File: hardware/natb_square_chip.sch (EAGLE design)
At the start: 8 parts, among them U1 TINY212, U2 MEGA32U4-MU

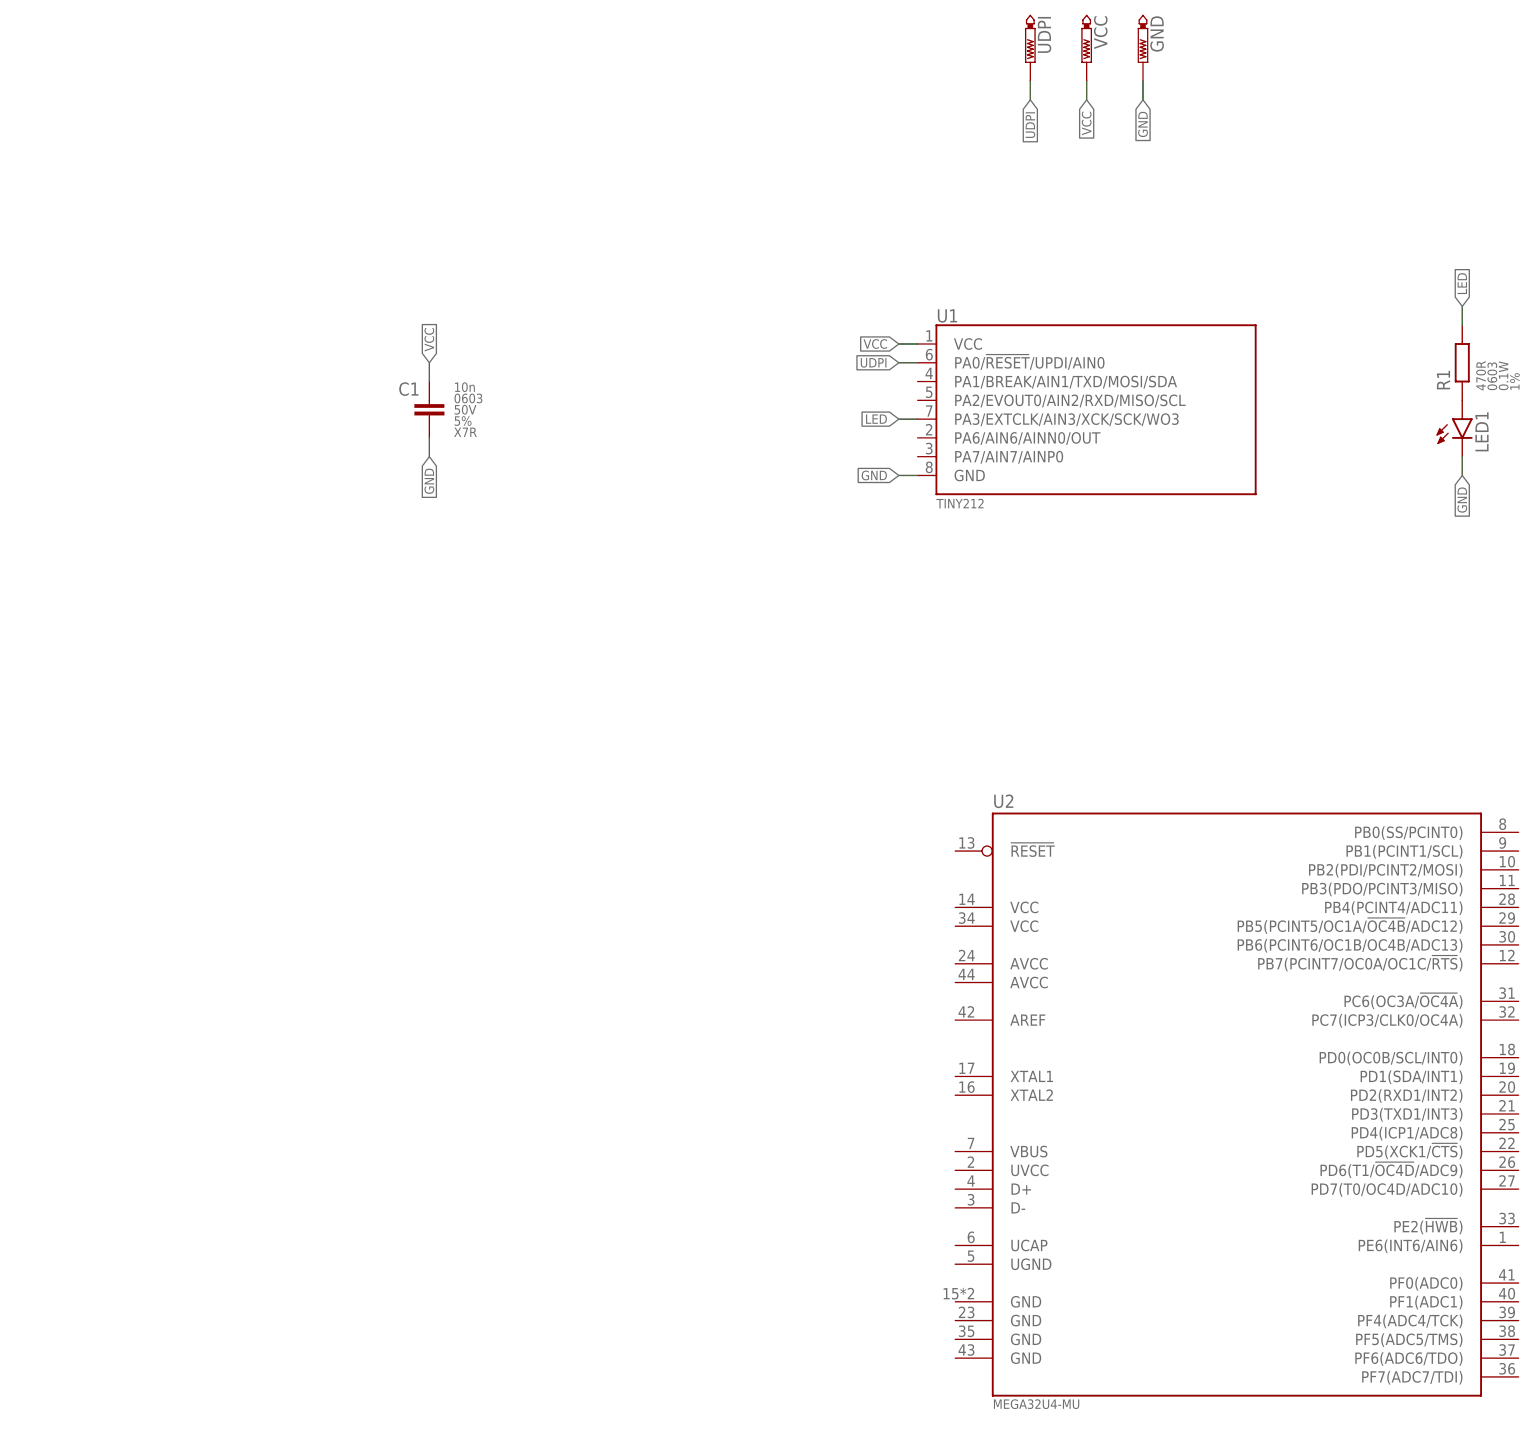
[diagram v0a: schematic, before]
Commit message: Changes SOIC and BGA
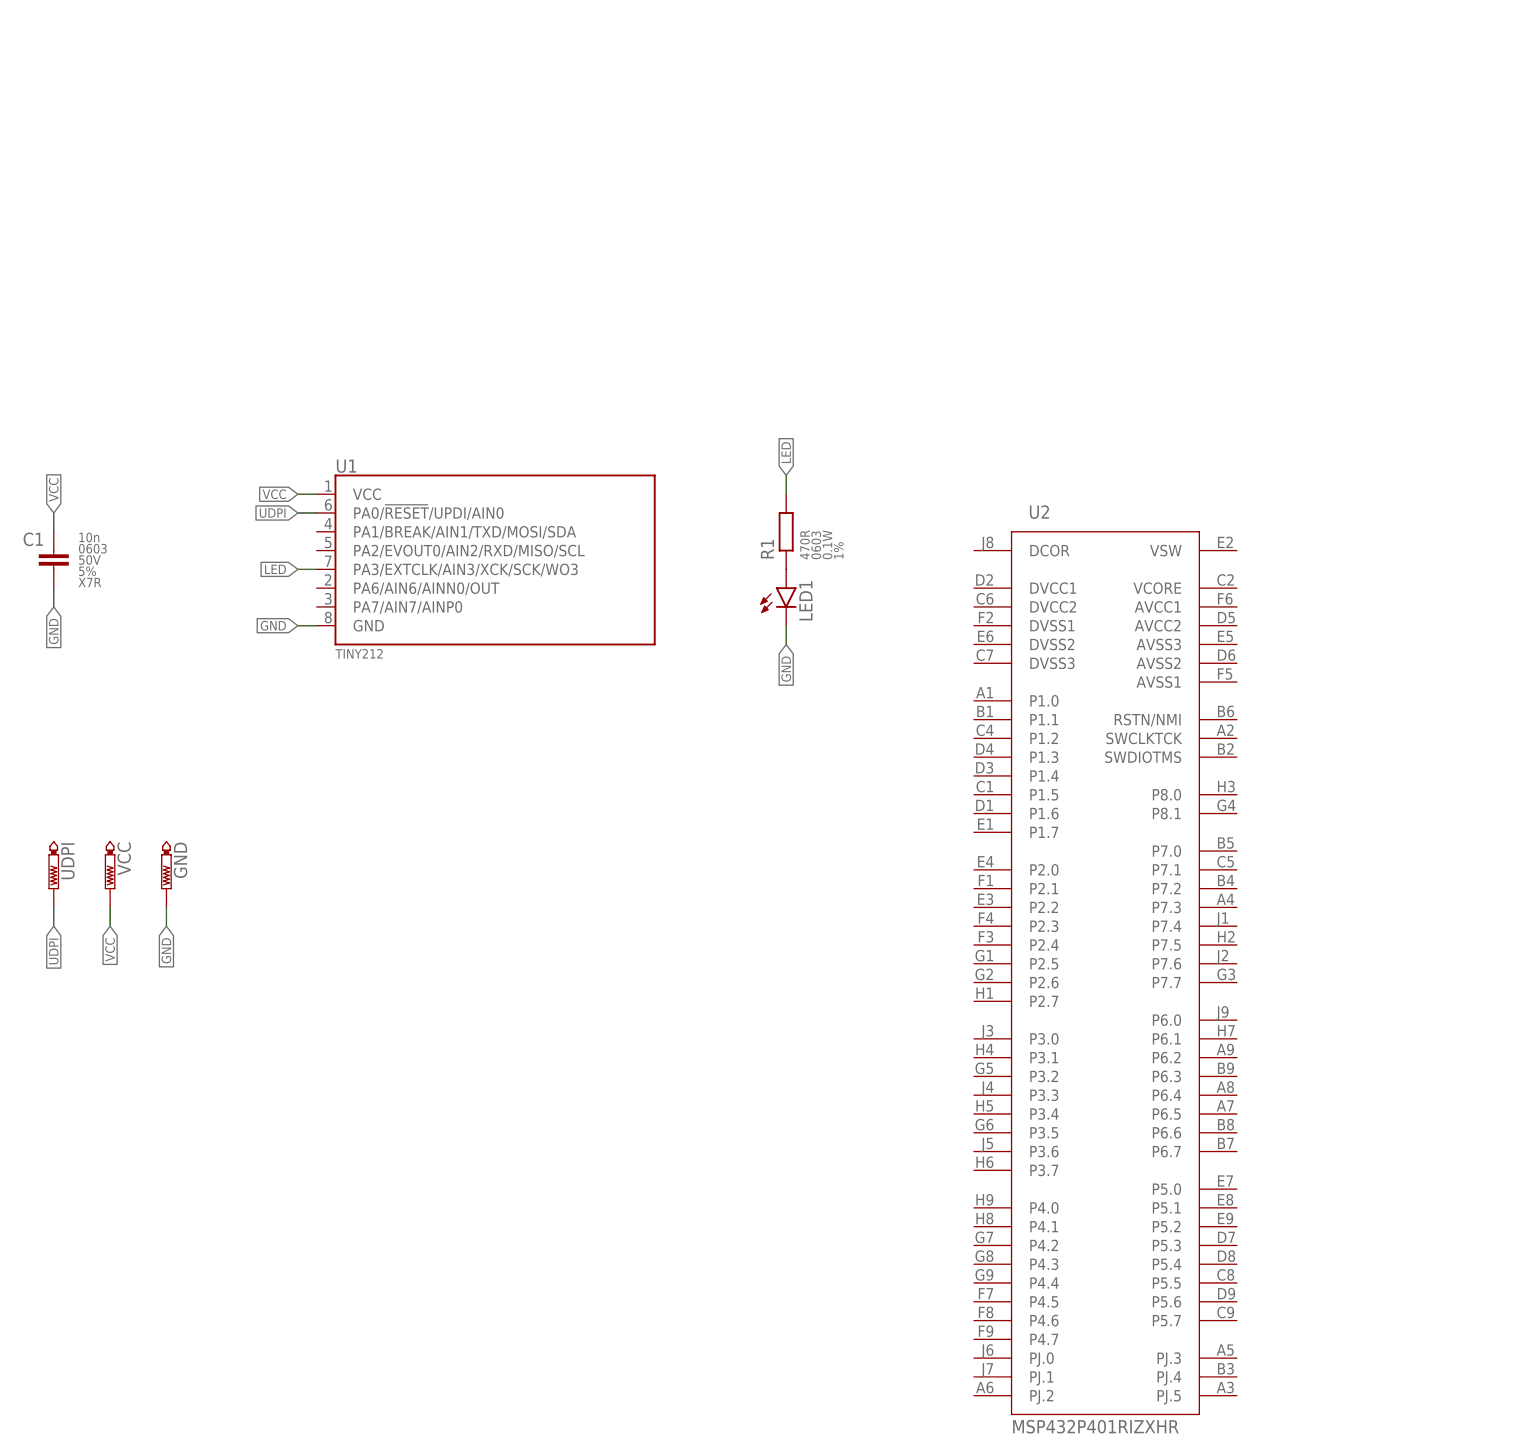
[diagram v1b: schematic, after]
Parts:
- U2: value MEGA32U4-MU -> MSP432P401RIZXHR; device zaan-IC-Microcontroller:MEGA32U4-MU -> Microcontroller:MSP432P401RIZXHR
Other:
- moved on the sheet: C1, GND, LED1, R1, U1, UDPI, VCC

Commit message: Changed parts and added qr code
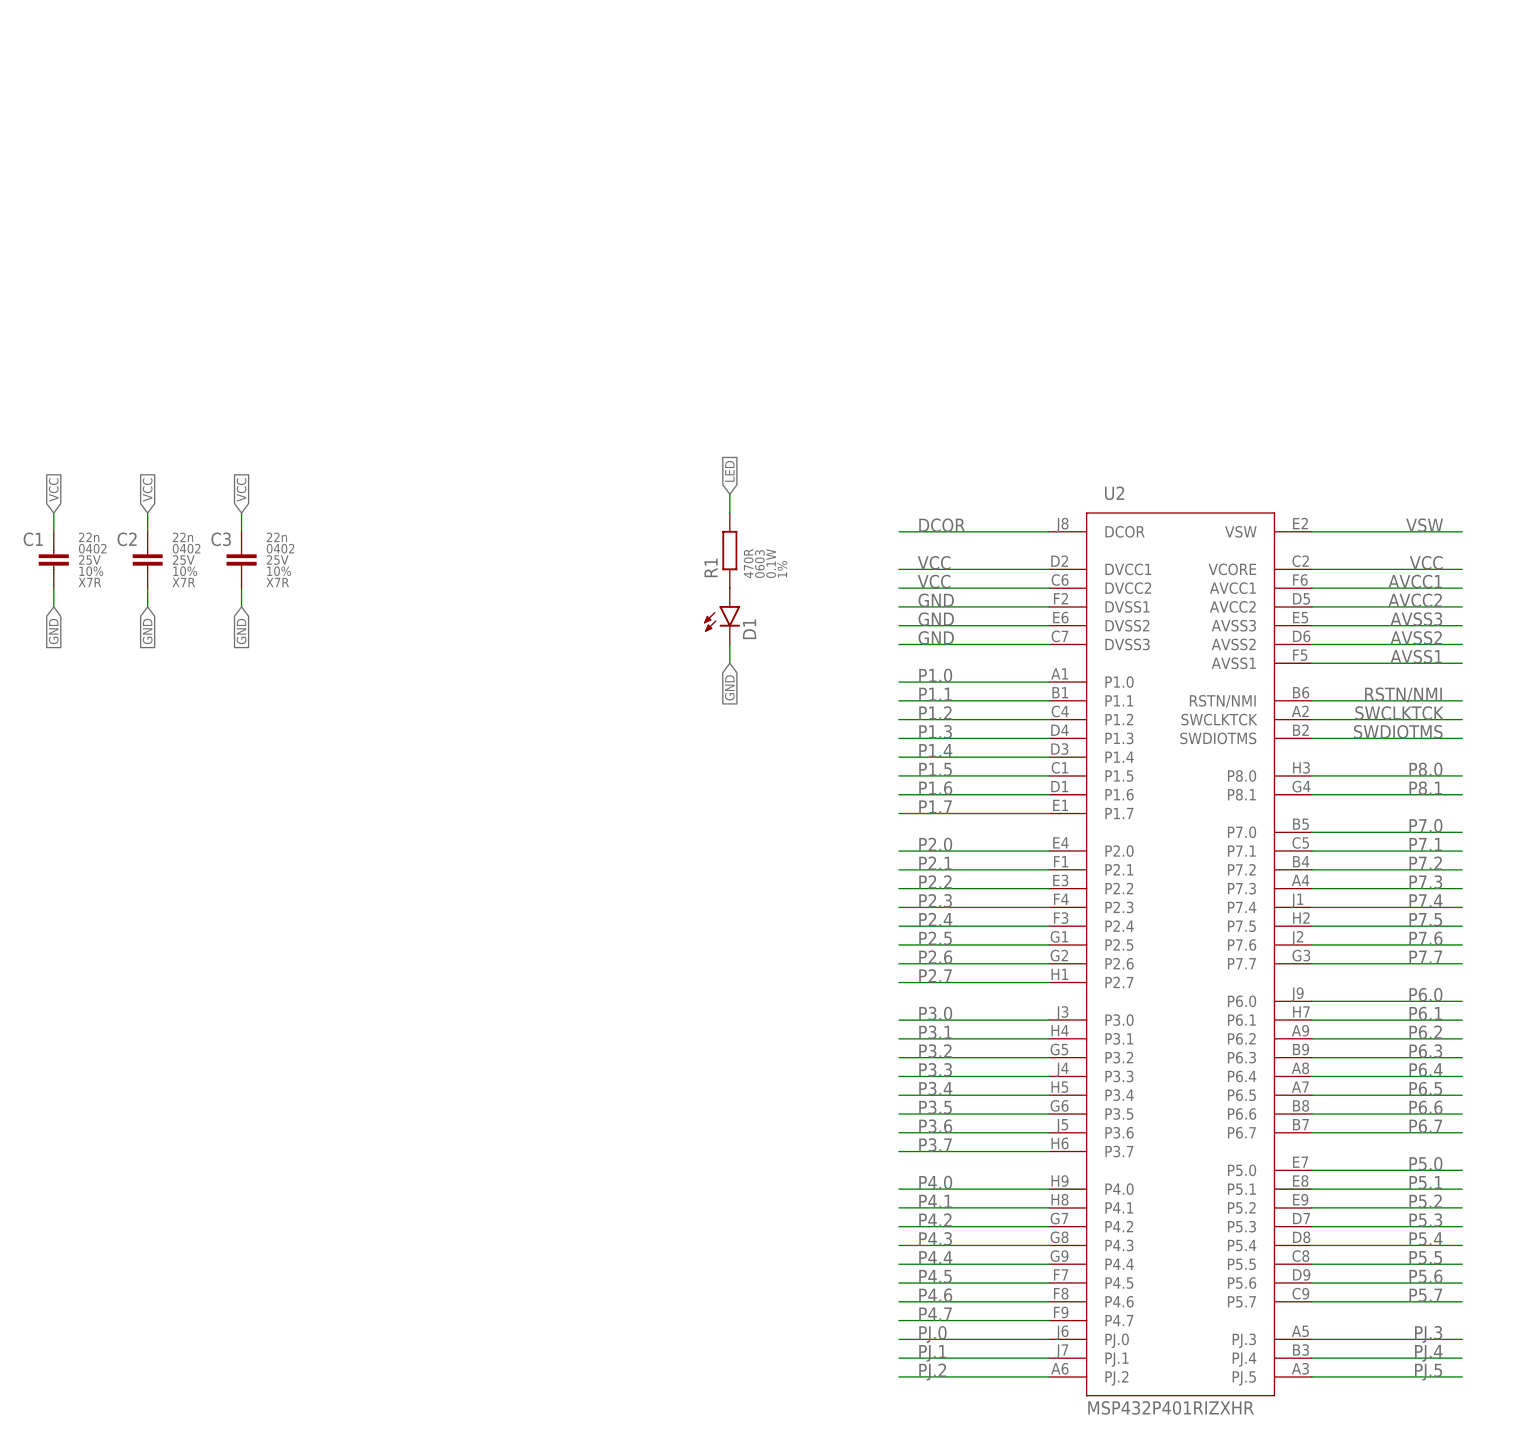
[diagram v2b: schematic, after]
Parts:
- removed GND, UDPI, VCC: PTR1B1,27, testpad:PTR1B1,27
- removed LED1: (no value), led:LEDCHIP-LED0603
- removed U1: TINY212, zaan-IC-Microcontroller:TINY212
- added C2, C3: 22n, zaan-Capacitors:22NF-0402-25V-10%
- added D1: (no value), led:LEDCHIP-LED0603
- C1: value 10n -> 22n; device zaan-Capacitors:10NF-0603-50V-5% -> zaan-Capacitors:22NF-0402-25V-10%
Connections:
- removed net UDPI: U1.PA0/!RESET!/UPDI/AIN0, UDPI.TP
- new net AVCC1: U2.AVCC1
- new net AVCC2: U2.AVCC2
- new net AVSS1: U2.AVSS1
- new net AVSS2: U2.AVSS2
- new net AVSS3: U2.AVSS3
- new net DCOR: U2.DCOR
- new net P1.0: U2.P1.0
- new net P1.1: U2.P1.1
- new net P1.2: U2.P1.2
- new net P1.3: U2.P1.3
- new net P1.4: U2.P1.4
- new net P1.5: U2.P1.5
- new net P1.6: U2.P1.6
- new net P1.7: U2.P1.7
- new net P2.0: U2.P2.0
- new net P2.1: U2.P2.1
- new net P2.2: U2.P2.2
- new net P2.3: U2.P2.3
- new net P2.4: U2.P2.4
- new net P2.5: U2.P2.5
- new net P2.6: U2.P2.6
- new net P2.7: U2.P2.7
- new net P3.0: U2.P3.0
- new net P3.1: U2.P3.1
- new net P3.2: U2.P3.2
- new net P3.3: U2.P3.3
- new net P3.4: U2.P3.4
- new net P3.5: U2.P3.5
- new net P3.6: U2.P3.6
- new net P3.7: U2.P3.7
- new net P4.0: U2.P4.0
- new net P4.1: U2.P4.1
- new net P4.2: U2.P4.2
- new net P4.3: U2.P4.3
- new net P4.4: U2.P4.4
- new net P4.5: U2.P4.5
- new net P4.6: U2.P4.6
- new net P4.7: U2.P4.7
- new net P5.0: U2.P5.0
- new net P5.1: U2.P5.1
- new net P5.2: U2.P5.2
- new net P5.3: U2.P5.3
- new net P5.4: U2.P5.4
- new net P5.5: U2.P5.5
- new net P5.6: U2.P5.6
- new net P5.7: U2.P5.7
- new net P6.0: U2.P6.0
- new net P6.1: U2.P6.1
- new net P6.2: U2.P6.2
- new net P6.3: U2.P6.3
- new net P6.4: U2.P6.4
- new net P6.5: U2.P6.5
- new net P6.6: U2.P6.6
- new net P6.7: U2.P6.7
- new net P7.0: U2.P7.0
- new net P7.1: U2.P7.1
- new net P7.2: U2.P7.2
- new net P7.3: U2.P7.3
- new net P7.4: U2.P7.4
- new net P7.5: U2.P7.5
- new net P7.6: U2.P7.6
- new net P7.7: U2.P7.7
- new net P8.0: U2.P8.0
- new net P8.1: U2.P8.1
- new net PJ.0: U2.PJ.0
- new net PJ.1: U2.PJ.1
- new net PJ.2: U2.PJ.2
- new net PJ.3: U2.PJ.3
- new net PJ.4: U2.PJ.4
- new net PJ.5: U2.PJ.5
- new net RSTN/NMI: U2.RSTN/NMI
- new net SWCLKTCK: U2.SWCLKTCK
- new net SWDIOTMS: U2.SWDIOTMS
- new net VSW: U2.VSW
- net GND: now also C2.2, C3.2, D1.C, U2.DVSS1, U2.DVSS2, U2.DVSS3; no longer GND.TP, LED1.C, U1.GND
- net LED: no longer U1.PA3/EXTCLK/AIN3/XCK/SCK/WO3
- net N$1: now also D1.A; no longer LED1.A
- net VCC: now also C2.1, C3.1, U2.DVCC1, U2.DVCC2, U2.VCORE; no longer U1.VCC, VCC.TP
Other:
- moved on the sheet: R1, U2
